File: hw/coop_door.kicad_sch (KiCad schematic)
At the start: 53 parts, among them J1 Screw_Terminal_01x02, J2 Screw_Terminal_01x02, J3 Screw_Terminal_01x02, Q1 Q_NMOS_DDGSDD, Q2 IRF4905, Q3 Q_NMOS_DDGSDD, Q4 Q_Dual_NMOS_S1G1D2S2G2D1, Q5 Q_PMOS_DDGSDD, SW1 SW_Push, SW2 SW_DPDT_x2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

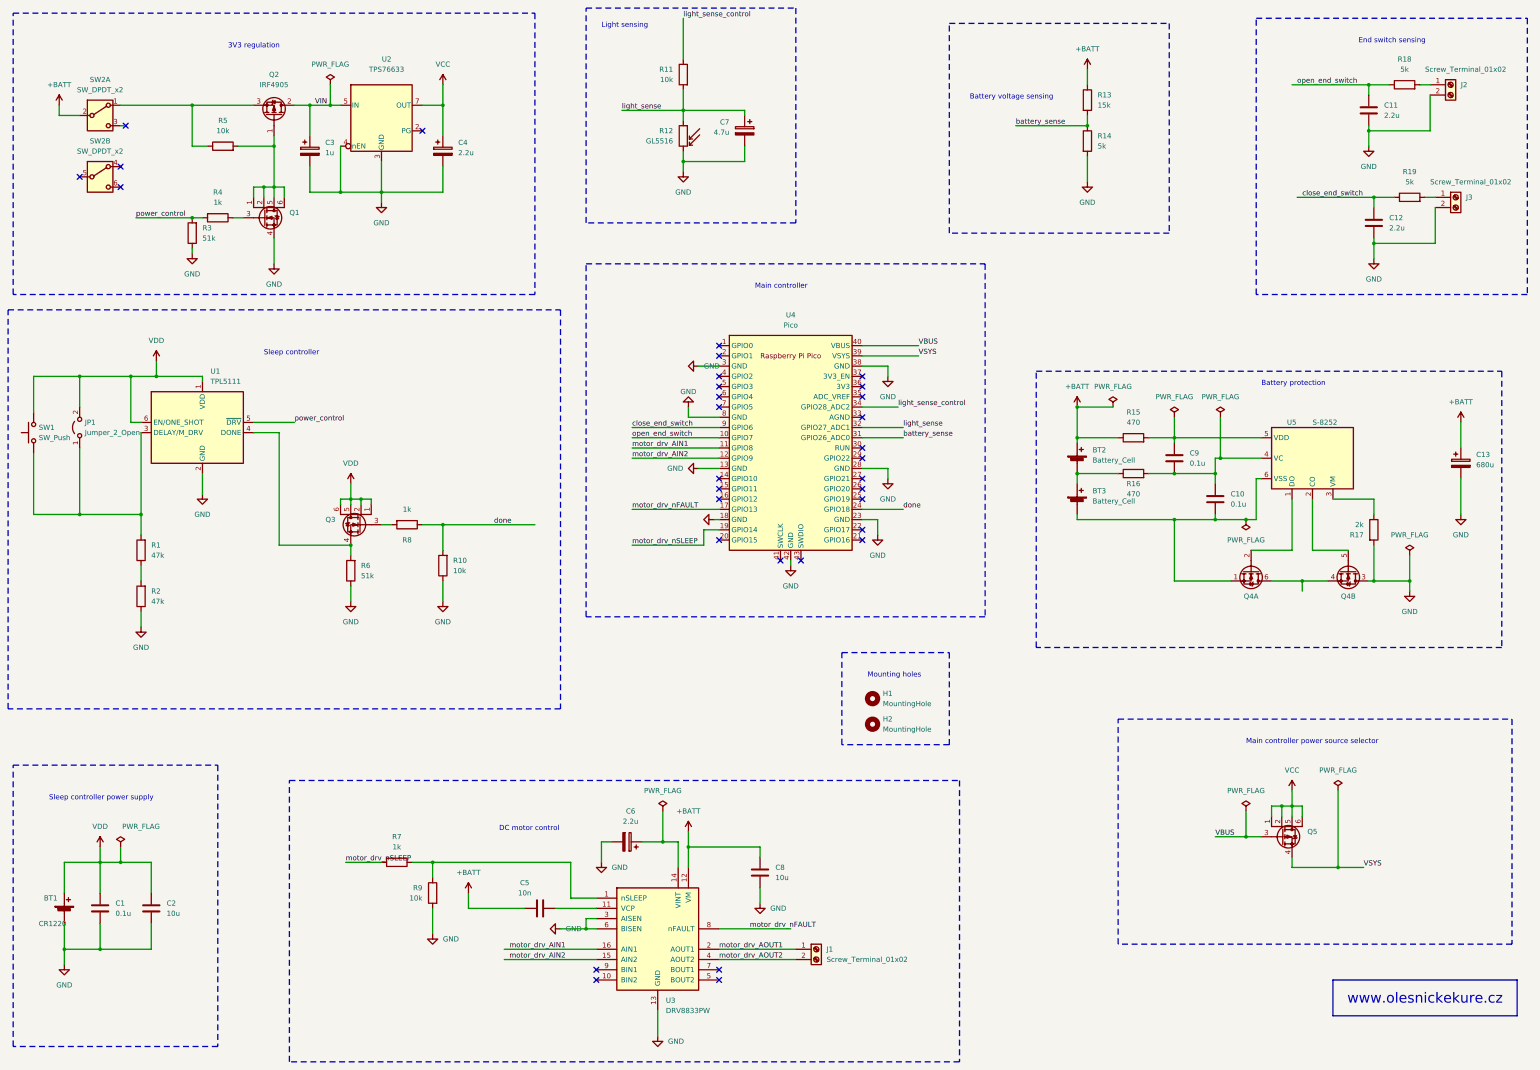
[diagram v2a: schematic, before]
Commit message: Transitor types
Show transitor types in the schematics
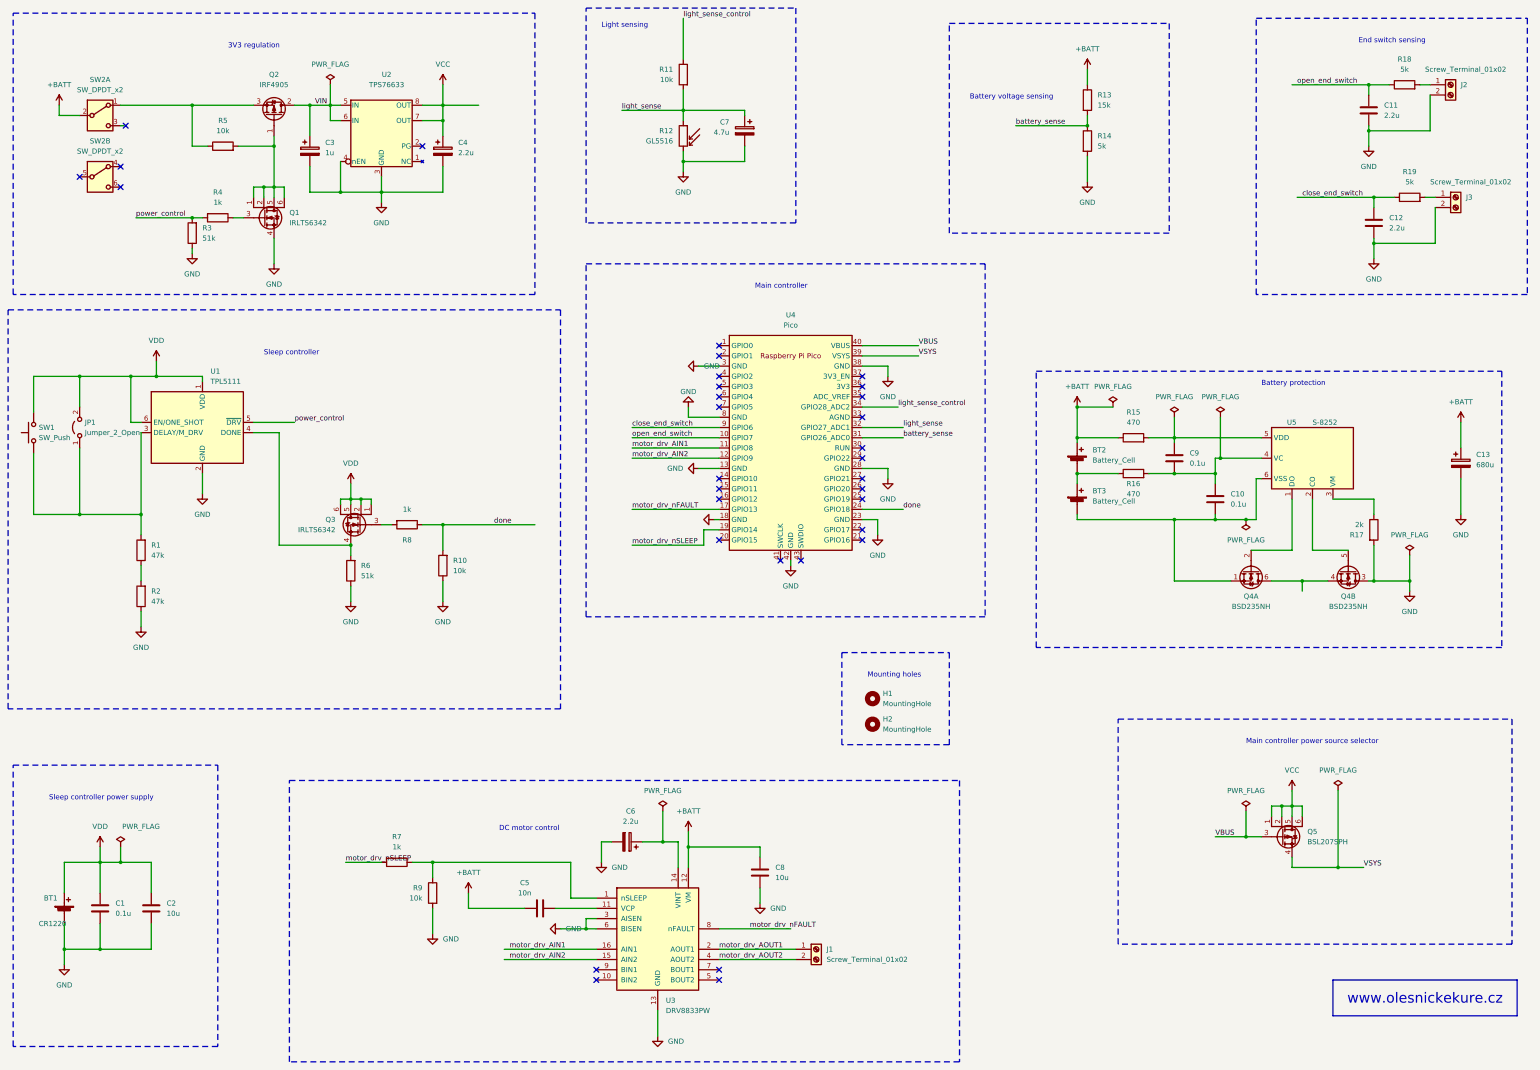
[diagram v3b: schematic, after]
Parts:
- Q1, Q3: value Q_NMOS_DDGSDD -> IRLTS6342
- Q4: value Q_Dual_NMOS_S1G1D2S2G2D1 -> BSD235NH
- Q5: value Q_PMOS_DDGSDD -> BSL207SPH
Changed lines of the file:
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@@
   (junction (at 50.8 228.6) (diameter 0) (color 0 0 0 0)
   )
-  (junction (at 135.89 40.64) (diameter 0) (color 0 0 0 0)
-  )
   (junction (at 58.42 107.95) (diameter 0) (color 0 0 0 0)
   )
@@
   (junction (at 365.76 46.99) (diameter 0) (color 0 0 0 0)
   )
+  (junction (at 135.89 44.45) (diameter 0) (color 0 0 0 0)
+  )
   (junction (at 50.8 250.19) (diameter 0) (color 0 0 0 0)
   )
@@
   (junction (at 346.71 214.63) (diameter 0) (color 0 0 0 0)
   )
+  (junction (at 135.89 40.64) (diameter 0) (color 0 0 0 0)
+  )
   (junction (at 133.35 228.6) (diameter 0) (color 0 0 0 0)
   )
@@
   (no_connect (at 204.47 135.89))
   (no_connect (at 55.88 55.88))
-  (no_connect (at 130.81 46.99))
+  (no_connect (at 130.81 50.8))
   (no_connect (at 55.88 60.96))
   (no_connect (at 204.47 133.35))
@@
     (stroke (width 0) (type default))
   )
-  (wire (pts (xy 135.89 35.56) (xy 135.89 40.64))
+  (wire (pts (xy 135.89 40.64) (xy 135.89 35.56))
     (stroke (width 0) (type default))
   )
@@
     (stroke (width 0) (type default))
   )
-  (wire (pts (xy 130.81 40.64) (xy 135.89 40.64))
+  (wire (pts (xy 130.81 44.45) (xy 135.89 44.45))
     (stroke (width 0) (type default))
   )
@@
     (stroke (width 0) (type default))
   )
-  (wire (pts (xy 120.65 54.61) (xy 120.65 62.23))
+  (wire (pts (xy 120.65 58.42) (xy 120.65 62.23))
     (stroke (width 0) (type default))
   )
@@
     (stroke (width 0) (type default))
   )
+  (wire (pts (xy 135.89 44.45) (xy 135.89 48.26))
+    (stroke (width 0) (type default))
+  )
   (wire (pts (xy 60.96 142.24) (xy 60.96 147.32))
     (stroke (width 0) (type default))
@@
     (stroke (width 0) (type default))
   )
+  (wire (pts (xy 130.81 40.64) (xy 135.89 40.64))
+    (stroke (width 0) (type default))
+  )
   (wire (pts (xy 41.91 243.84) (xy 41.91 250.19))
     (stroke (width 0) (type default))
@@
     (stroke (width 0) (type default))
   )
+  (wire (pts (xy 110.49 44.45) (xy 107.95 44.45))
+    (stroke (width 0) (type default))
+  )
   (wire (pts (xy 93.98 60.96) (xy 91.44 60.96))
     (stroke (width 0) (type default))
@@
     (stroke (width 0) (type default))
   )
+  (wire (pts (xy 135.89 40.64) (xy 144.78 40.64))
+    (stroke (width 0) (type default))
+  )
   (wire (pts (xy 34.29 116.84) (xy 34.29 107.95))
     (stroke (width 0) (type default))
@@
     (stroke (width 0) (type default))
   )
-  (wire (pts (xy 135.89 40.64) (xy 135.89 48.26))
+  (wire (pts (xy 135.89 44.45) (xy 135.89 40.64))
     (stroke (width 0) (type default))
   )
@@
     (stroke (width 0) (type default))
   )
-  (wire (pts (xy 110.49 50.8) (xy 110.49 62.23))
+  (wire (pts (xy 110.49 54.61) (xy 110.49 62.23))
     (stroke (width 0) (type default))
   )
@@
     (stroke (width 0) (type default))
   )
+  (wire (pts (xy 107.95 44.45) (xy 107.95 40.64))
+    (stroke (width 0) (type default))
+  )
   (wire (pts (xy 370.84 35.56) (xy 365.76 35.56))
     (stroke (width 0) (type default))
@@
       (effects (font (size 1.27 1.27)) (justify left))
     )
-    (property "Value" "Q_NMOS_DDGSDD" (at 97.79 69.85 0)
-      (effects (font (size 1.27 1.27)) (justify left) hide)
+    (property "Value" "IRLTS6342" (at 97.79 69.85 0)
+      (effects (font (size 1.27 1.27)) (justify left))
     )
     (property "Footprint" "Package_SO:TSOP-6_1.65x3.05mm_P0.95mm" (at 96.52 66.04 0)
@@
       (effects (font (size 1.27 1.27)))
     )
-    (property "Value" "Q_Dual_NMOS_S1G1D2S2G2D1" (at 336.55 165.1 90)
-      (effects (font (size 1.27 1.27)) hide)
+    (property "Value" "BSD235NH" (at 336.55 165.1 90)
+      (effects (font (size 1.27 1.27)))
     )
     (property "Footprint" "Package_TO_SOT_SMD:SOT-363_SC-70-6_Handsoldering" (at 336.55 161.29 0)
@@
       (effects (font (size 1.27 1.27)) (justify left))
     )
-    (property "Value" "Q_PMOS_DDGSDD" (at 350.52 223.52 0)
-      (effects (font (size 1.27 1.27)) (justify left) hide)
+    (property "Value" "BSL207SPH" (at 350.52 223.52 0)
+      (effects (font (size 1.27 1.27)) (justify left))
     )
     (property "Footprint" "Package_SO:TSOP-6_1.65x3.05mm_P0.95mm" (at 349.25 219.71 0)
@@
       (effects (font (size 1.27 1.27)))
     )
-    (property "Value" "Q_Dual_NMOS_S1G1D2S2G2D1" (at 360.68 165.1 90)
-      (effects (font (size 1.27 1.27)) hide)
+    (property "Value" "BSD235NH" (at 360.68 165.1 90)
+      (effects (font (size 1.27 1.27)))
     )
     (property "Footprint" "Package_TO_SOT_SMD:SOT-363_SC-70-6_Handsoldering" (at 360.68 161.29 0)
@@
     )
   )
-  (symbol (lib_id "coop_door_library:TPS76633") (at 120.65 40.64 0) (unit 1)
-    (in_bom yes) (on_board yes) (dnp no) (fields_autoplaced)
-    (property "Reference" "U2" (at 121.92 29.21 0)
+  (symbol (lib_id "coop_door_library:TPS76633") (at 120.65 44.45 0) (unit 1)
+    (in_bom yes) (on_board yes) (dnp no)
+    (property "Reference" "U2" (at 121.92 33.02 0)
       (effects (font (size 1.27 1.27)))
     )
-    (property "Value" "TPS76633" (at 121.92 31.75 0)
+    (property "Value" "TPS76633" (at 121.92 35.56 0)
       (effects (font (size 1.27 1.27)))
     )
-    (property "Footprint" "Package_SO:SOIC-8-1EP_3.9x4.9mm_P1.27mm_EP2.514x3.2mm" (at 124.46 26.67 0)
+    (property "Footprint" "Package_SO:SOIC-8-1EP_3.9x4.9mm_P1.27mm_EP2.514x3.2mm" (at 124.46 30.48 0)
       (effects (font (size 1.27 1.27) italic) hide)
     )
-    (property "Datasheet" "https://www.ti.com/lit/ds/symlink/tps766.pdf" (at 124.46 52.07 0)
+    (property "Datasheet" "https://www.ti.com/lit/ds/symlink/tps766.pdf" (at 124.46 55.88 0)
       (effects (font (size 1.27 1.27)) hide)
     )
@@
       (effects (font (size 1.27 1.27)) (justify left))
     )
-    (property "Value" "Q_NMOS_DDGSDD" (at 109.22 146.05 0)
-      (effects (font (size 1.27 1.27)) (justify left) hide)
+    (property "Value" "IRLTS6342" (at 109.22 146.05 0)
+      (effects (font (size 1.27 1.27)) (justify left))
     )
     (property "Footprint" "Package_SO:TSOP-6_1.65x3.05mm_P0.95mm" (at 110.49 142.24 0)

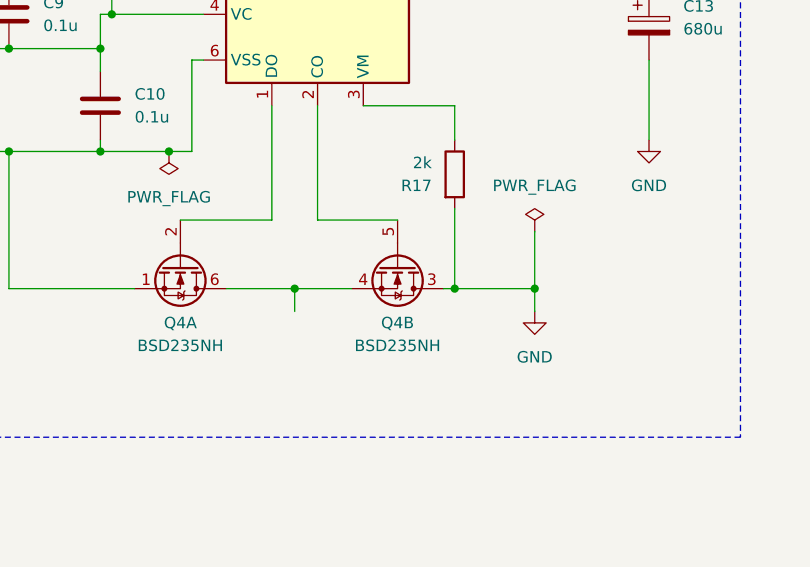
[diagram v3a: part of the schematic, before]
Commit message: PCB fixes
- Fix the battery protection IC MOSFET connections
- Add the main switch ON/OFF silkscreen labels
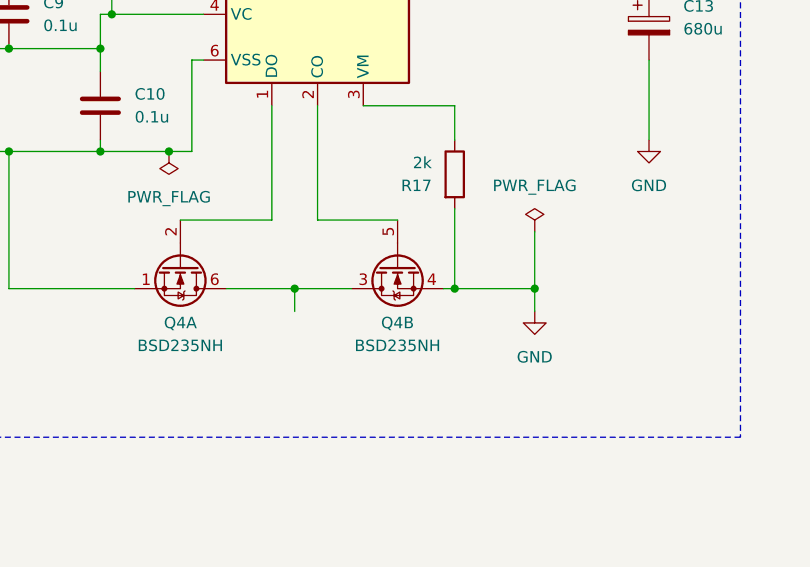
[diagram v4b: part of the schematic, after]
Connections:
- net GND: now also Q4.4 (S); no longer Q4.3 (D)
- net at Q4.6 (D): now also Q4.3 (D); no longer Q4.4 (S)
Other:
- moved on the sheet: Q4B
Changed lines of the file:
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@@
   (junction (at 317.5 123.19) (diameter 0) (color 0 0 0 0)
   )
+  (junction (at 367.03 158.75) (diameter 0) (color 0 0 0 0)
+  )
   (junction (at 55.88 228.6) (diameter 0) (color 0 0 0 0)
   )
@@
   (junction (at 195.58 41.91) (diameter 0) (color 0 0 0 0)
   )
-  (junction (at 349.25 158.75) (diameter 0) (color 0 0 0 0)
-  )
   (junction (at 115.57 138.43) (diameter 0) (color 0 0 0 0)
   )
@@
   (junction (at 293.37 132.08) (diameter 0) (color 0 0 0 0)
   )
-  (junction (at 367.03 158.75) (diameter 0) (color 0 0 0 0)
-  )
   (junction (at 346.71 214.63) (diameter 0) (color 0 0 0 0)
   )
@@
   (junction (at 133.35 228.6) (diameter 0) (color 0 0 0 0)
   )
+  (junction (at 349.25 158.75) (diameter 0) (color 0 0 0 0)
+  )
   (junction (at 45.72 107.95) (diameter 0) (color 0 0 0 0)
   )
@@
     (stroke (width 0) (type default))
   )
-  (wire (pts (xy 349.25 158.75) (xy 355.6 158.75))
-    (stroke (width 0) (type default))
-  )
   (wire (pts (xy 240.03 100.33) (xy 254 100.33))
     (stroke (width 0) (type default))
@@
     (stroke (width 0) (type default))
   )
+  (wire (pts (xy 365.76 158.75) (xy 367.03 158.75))
+    (stroke (width 0) (type default))
+  )
   (wire (pts (xy 337.82 133.35) (xy 339.09 133.35))
     (stroke (width 0) (type default))
@@
     (stroke (width 0) (type default))
   )
-  (wire (pts (xy 367.03 158.75) (xy 365.76 158.75))
-    (stroke (width 0) (type default))
-  )
   (wire (pts (xy 167.64 228.6) (xy 133.35 228.6))
     (stroke (width 0) (type default))
@@
     (stroke (width 0) (type default))
   )
+  (wire (pts (xy 349.25 158.75) (xy 355.6 158.75))
+    (stroke (width 0) (type default))
+  )
   (wire (pts (xy 317.5 118.11) (xy 317.5 123.19))
     (stroke (width 0) (type default))
@@
     )
   )
-  (symbol (lib_id "Device:Q_Dual_NMOS_S1G1D2S2G2D1") (at 360.68 156.21 270) (unit 2)
-    (in_bom yes) (on_board yes) (dnp no) (fields_autoplaced)
+  (symbol (lib_id "Device:Q_Dual_NMOS_S1G1D2S2G2D1") (at 360.68 156.21 90) (mirror x) (unit 2)
+    (in_bom yes) (on_board yes) (dnp no)
     (property "Reference" "Q4" (at 360.68 162.56 90)
       (effects (font (size 1.27 1.27)))
